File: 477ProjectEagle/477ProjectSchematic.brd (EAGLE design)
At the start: 101.6 x 76.2 mm, 67 parts, among them J1 POWER_JACK_BAT, J2 POWER_JACK_12VOUT, Q1 AO4419, X1 22-23-2051, X10 22-23-2041, X2 XRJK-S-01-6-6-0-2G2-NO

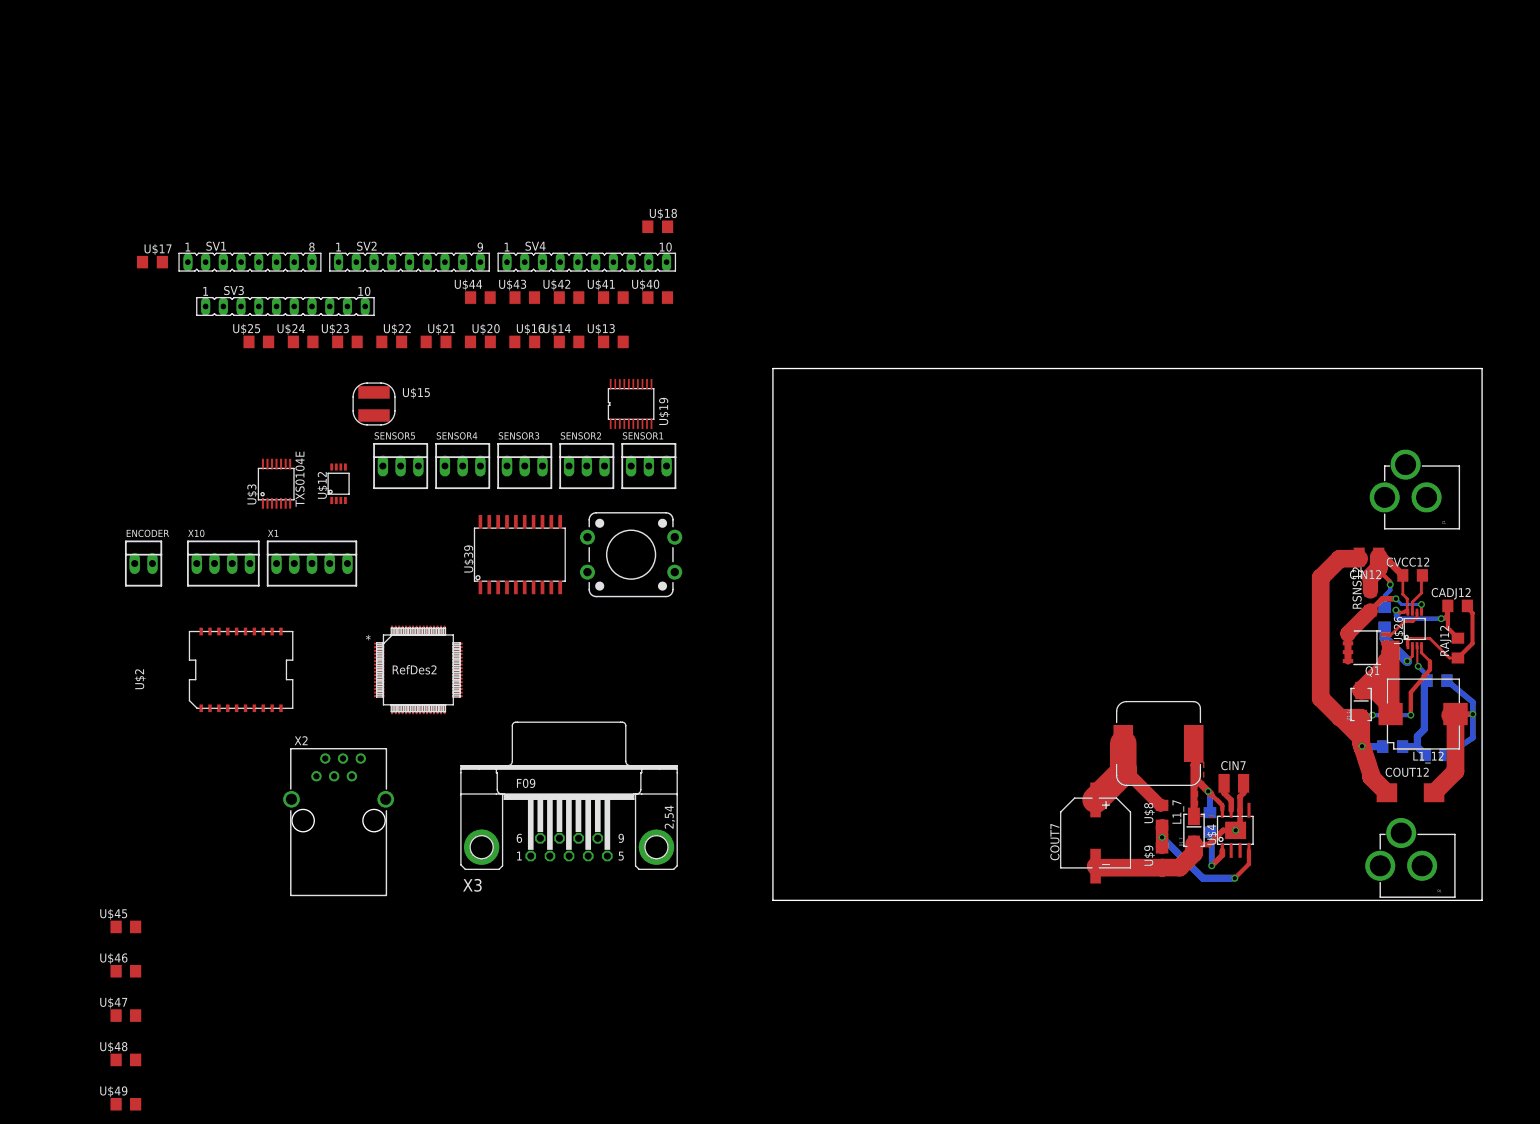
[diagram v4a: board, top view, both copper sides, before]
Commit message: Scott from lab -- worked on main PCB
Got all of the power supply circuits hooked up. Need to review them a
little bit more to make sure all traces are large enough etc...The board
is now 4 inches by 5 inches. That seems to be big enough
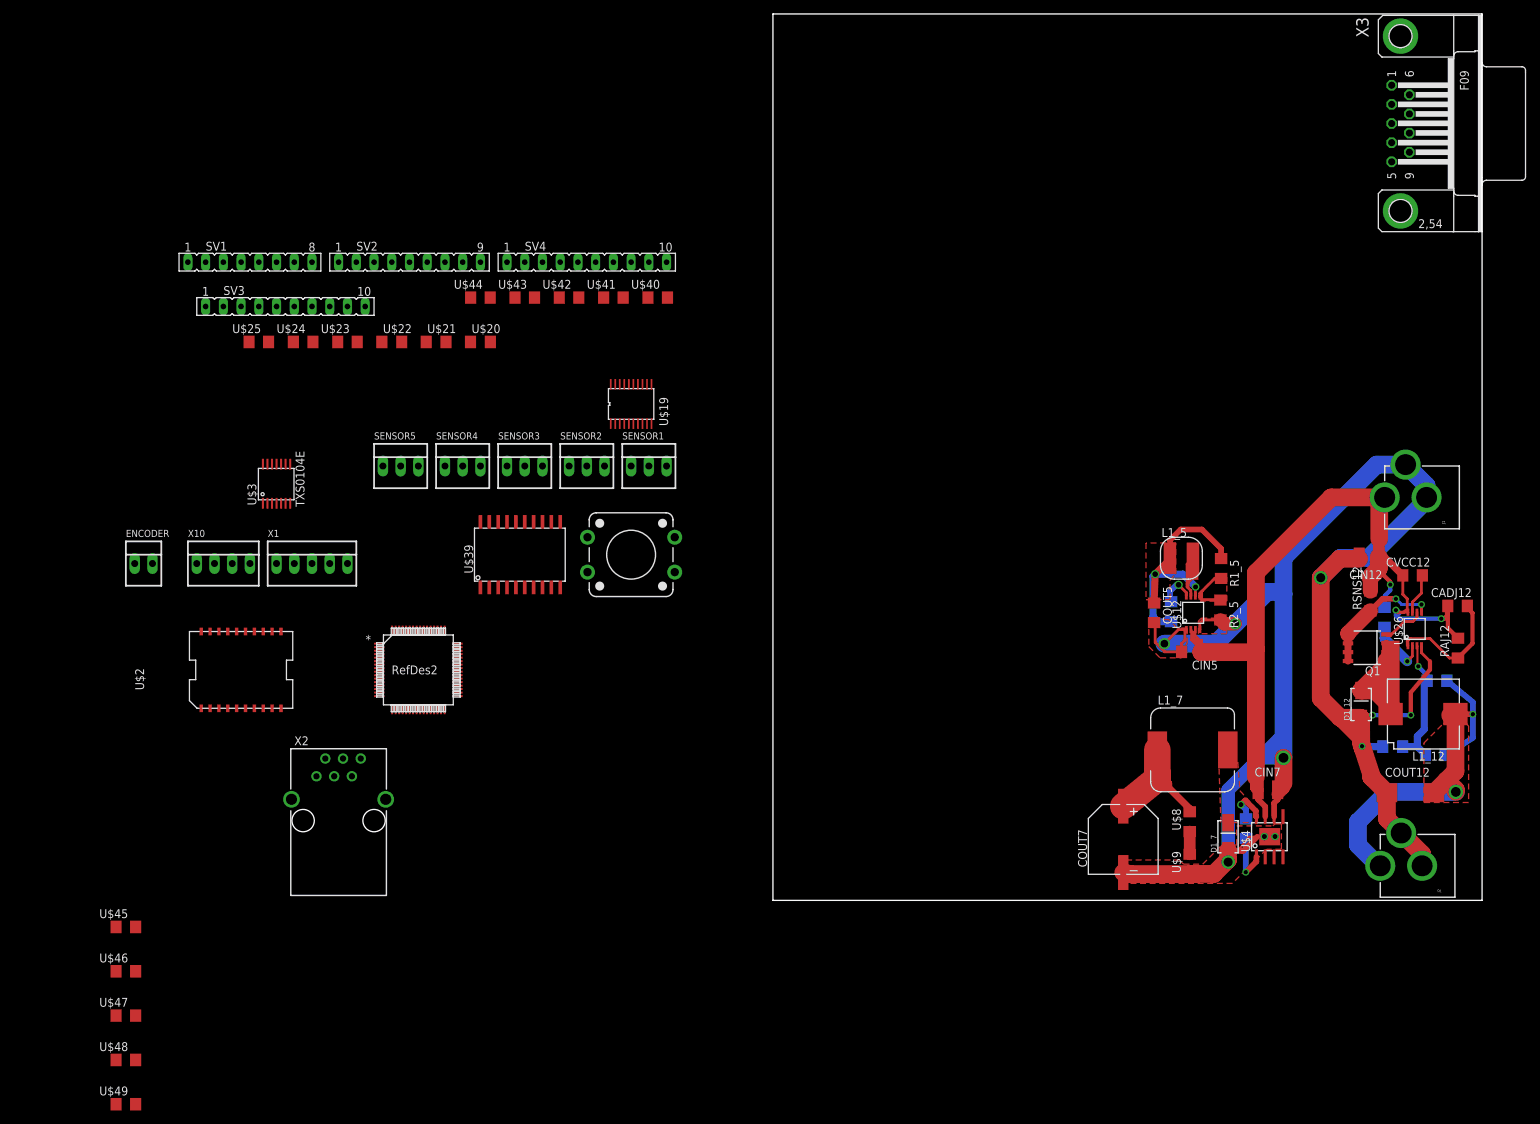
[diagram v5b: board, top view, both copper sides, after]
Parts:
- removed U$13: 10uF, MinotaurParts:C1206
- removed U$14: 22uF, MinotaurParts:C1206
- removed U$15: 2.2uH, MinotaurParts:SDR0403
- removed U$17, U$18: (no value), MinotaurParts:R1206
- added CIN5: 10uF, MinotaurParts:C1206
- added COUT5: 22uF, MinotaurParts:C1206
- added L1_5: 2.2uH, MinotaurParts:SDR0403
- added R1_5, R2_5: (no value), MinotaurParts:R1206
- moved X3 157.9 mm to (89.9, 111.3), turned to 270 degrees
- moved U$12 123.8 mm to (60.2, 41.2)
- moved U$16 100.4 mm to (57.0, 41.4), flipped to the bottom, turned to 90 degrees
- moved CBOOT7 5.26 mm to (67.8, 10.3)
- moved D1_7 4.96 mm to (65.2, 9.12)
- moved L1_7 4.96 mm to (60.1, 21.6)
- moved U$4 4.96 mm to (71.2, 9.12)
- moved CIN7 4.96 mm to (70.9, 15.8)
- moved U$8 4.07 mm to (59.7, 11.3)
- moved U$9 4.07 mm to (59.7, 5.18)
- moved COUT7 4.07 mm to (50.2, 8.74)
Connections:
- net +5V: now also COUT5.1, L1_5.B, R1_5.1; no longer U$14.1, U$15.B, U$17.1
- net GND: now also CIN5.2, COUT5.2, R2_5.2; no longer U$13.2, U$14.2, U$18.2
- net N$36: now also L1_5.A; no longer U$15.A
- net N$40: now also R1_5.2, R2_5.1; no longer U$17.2, U$18.1
- net V+: now also CIN5.1; no longer U$13.1
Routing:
- net GND: track 100.2 -> 267.6 mm, vias 4 -> 8
- net V+: track 44.0 -> 123.2 mm
- net +5V: track 0.00 -> 37.4 mm, vias 0 -> 2
- net +12V: track 31.4 -> 57.1 mm, vias 1 -> 2
- net N$28: track 20.9 -> 3.25 mm, vias 2 -> 0
- net N$16: track 22.4 -> 6.22 mm
- net N$40: track 0.00 -> 8.54 mm
- net N$36: track 0.00 -> 8.53 mm
- net N$37: track 0.00 -> 5.26 mm, vias 0 -> 1
- net +7V: track 17.5 -> 21.2 mm
- added copper zone on layer 1, net +12V
- added copper zone on layer 1, net +5V
- added copper zone on layer 1, net GND
- added copper zone on layer 1, net N$40
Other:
- board size 101.6 x 76.2 mm -> 101.6 x 127 mm

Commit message: Continued work on main PCB
All components are in a rough position on the board. Everything just
needs to be connected now...
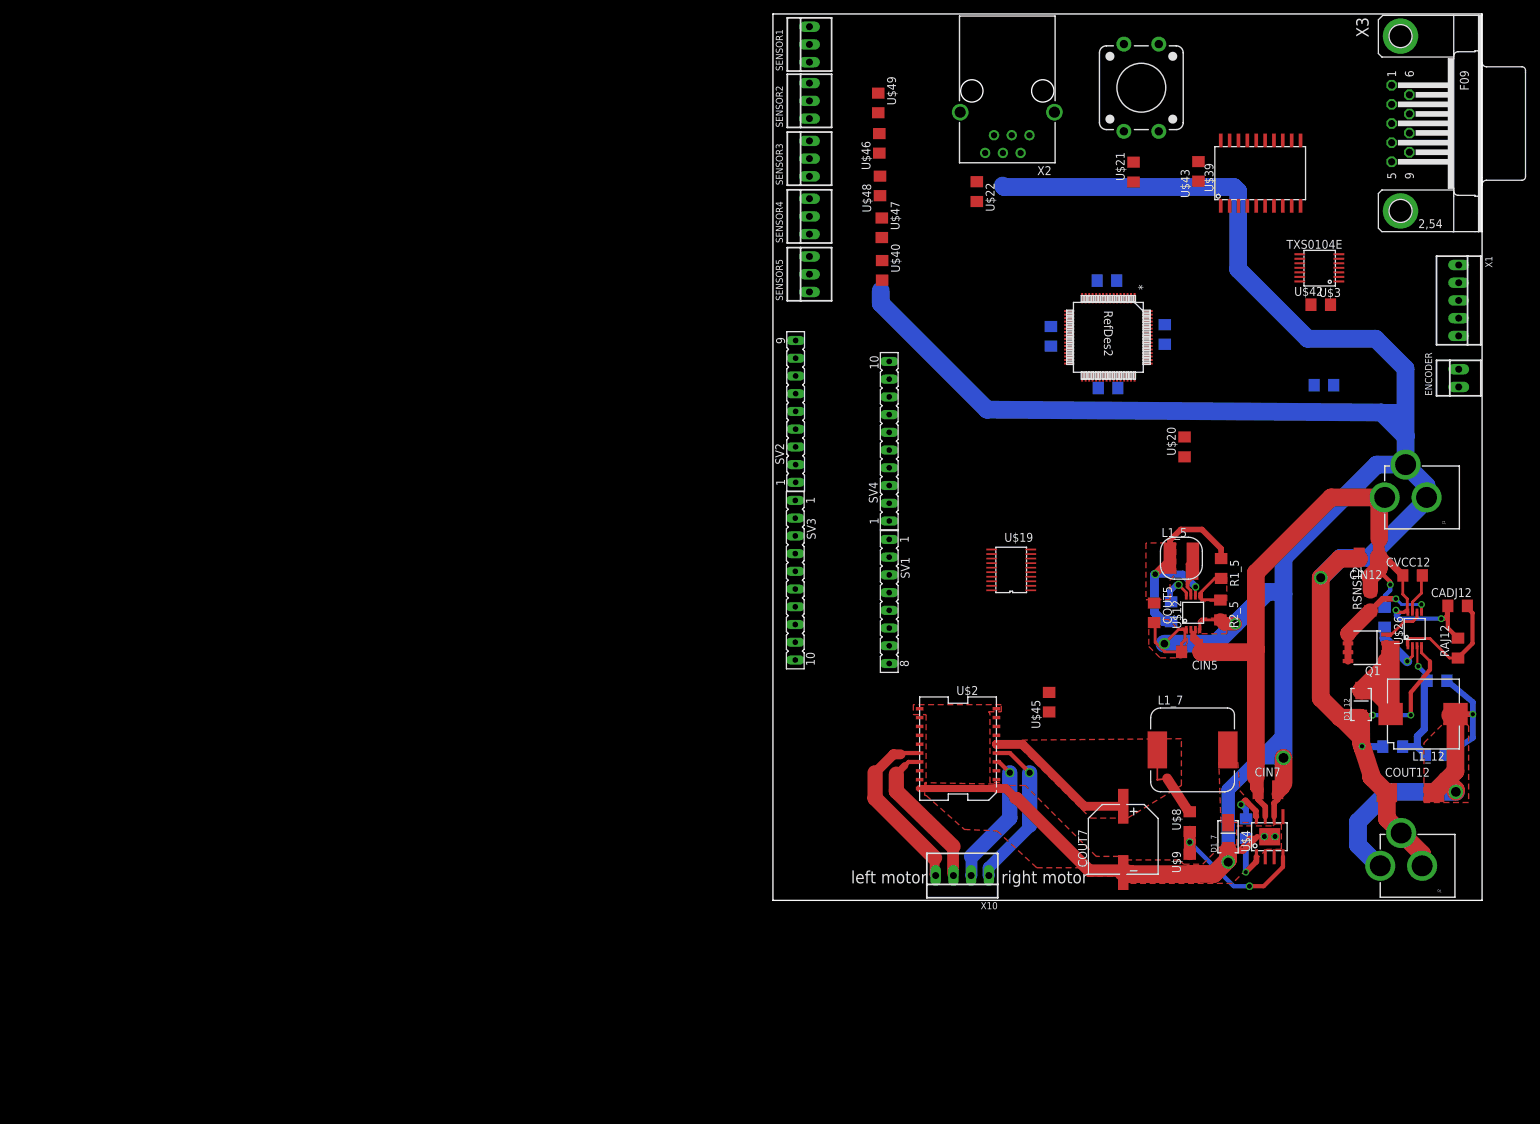
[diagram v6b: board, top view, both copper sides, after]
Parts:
- X10: value 22-23-2041 -> MOTORS
- moved ENCODER 190.3 mm to (98.2, 74.8), turned to 90 degrees
- moved U$49 179.4 mm to (15.1, 114.2), turned to 270 degrees
- moved X1 168.6 mm to (98.2, 86.0), turned to 270 degrees
- moved U$48 165.4 mm to (15.3, 102.4), turned to 90 degrees
- moved U$46 160.4 mm to (15.2, 108.5), turned to 90 degrees
- moved U$47 156.4 mm to (15.6, 96.4), turned to 270 degrees
- moved U$25 152.7 mm to (78.9, 73.8), flipped to the bottom, turned to 180 degrees
- moved U$3 152.6 mm to (78.3, 90.6), turned to 90 degrees
- moved X2 141.8 mm to (33.6, 116.0), turned to 180 degrees
- moved U$45 136.1 mm to (39.6, 28.4), turned to 90 degrees
- moved U$39 119.3 mm to (70.5, 104.2)
- moved U$23 117.1 mm to (56.1, 81.1), flipped to the bottom, turned to 90 degrees
- moved U$24 115.5 mm to (48.0, 73.4), flipped to the bottom, turned to 180 degrees
- moved X10 114.9 mm to (27.1, 3.56), turned to 180 degrees
- moved U$1 109.7 mm to (48.1, 80.7), turned to 270 degrees
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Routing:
- net GND: track 267.6 -> 476.8 mm
- net N$21: track 0.00 -> 25.9 mm
- net N$19: track 0.00 -> 23.1 mm, vias 0 -> 1
- net N$20: track 0.00 -> 22.0 mm
- net N$18: track 0.00 -> 19.6 mm, vias 0 -> 1
- net N$28: track 3.25 -> 21.8 mm, vias 0 -> 2
- net +7V: track 21.2 -> 33.4 mm
- net +5V: track 37.4 -> 32.6 mm
- added copper zone on layer 1, net +7V
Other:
- board text added: "left motor"
- board text added: "right motor"

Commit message: Scott lab -- Work on main PCB
Started connecting everything together. Made a bunch of progress.
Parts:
- moved U$45 67.6 mm to (14.6, 91.2)
- moved U$40 58.6 mm to (73.7, 98.0), flipped to the bottom, turned to 180 degrees
- moved U$25 45.0 mm to (34.7, 82.0), turned to 90 degrees
- moved U$19 41.4 mm to (57.9, 81.3), turned to 270 degrees
- moved U$41 37.2 mm to (85.0, 87.6), flipped to the top
- moved U$23 17.2 mm to (39.3, 84.7), turned to 180 degrees
- moved U$43 16.5 mm to (60.7, 88.0)
- moved U$44 15.9 mm to (54.2, 87.8), flipped to the top
- moved U$20 12.5 mm to (50.2, 73.9), turned to 180 degrees
- moved U$46 11.3 mm to (14.6, 97.2)
- moved U$48 10.7 mm to (14.4, 113.0)
- moved U$1 10.7 mm to (37.4, 81.6)
- moved U$24 10.4 mm to (39.2, 78.9)
- moved U$42 10.0 mm to (86.6, 79.4), turned to 90 degrees
- moved U$3 9.87 mm to (81.6, 81.3), turned to 180 degrees
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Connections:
- net +3V3: now also X1.1; no longer X1.2
- net GND: now also X1.2; no longer X1.1
- net N$12: now also U$3.2
- net N$13: now also U$3.3
- net N$8: now also U$19.A8; no longer U$19.A7
- net N$9: now also U$19.A7; no longer U$19.A8
- net SCL: now also U$3.13
- net SDA: now also U$3.12
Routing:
- net +5V: track 32.6 -> 271.1 mm, vias 2 -> 8
- net GND: track 476.8 -> 674.4 mm, vias 8 -> 13
- net N$42: track 0.00 -> 72.4 mm
- net N$43: track 0.00 -> 69.9 mm
- net +3V3: track 0.00 -> 69.9 mm, vias 0 -> 1
- net N$41: track 0.00 -> 69.0 mm
- net N$44: track 0.00 -> 68.2 mm
- net N$45: track 0.00 -> 67.3 mm
- net N$39: track 0.00 -> 65.5 mm, vias 0 -> 2
- net N$12: track 0.00 -> 60.0 mm, vias 0 -> 2
- net N$13: track 0.00 -> 59.2 mm, vias 0 -> 2
- net N$1: track 0.00 -> 52.7 mm
- net N$2: track 0.00 -> 43.7 mm
- net SCL: track 0.00 -> 40.4 mm, vias 0 -> 1
- net N$3: track 0.00 -> 39.3 mm
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
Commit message: minor changes to main PCB
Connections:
- net N$85: now also U$1.51
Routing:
- net V+: track 123.2 -> 46.3 mm
- net N$5: track 27.0 -> 30.6 mm
- added copper zone on layer 1, net V+
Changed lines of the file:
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@@
 <wire x1="31.7754" y1="82.8294" x2="24.765" y2="82.8294" width="0.3048" layer="1"/>
 <wire x1="24.765" y1="82.8294" x2="17.9832" y2="89.6112" width="0.3048" layer="1"/>
-<wire x1="14.5796" y1="89.786" x2="17.9832" y2="89.6112" width="0" layer="19" extent="1-1"/>
+<wire x1="17.9832" y1="89.6112" x2="14.5796" y2="89.6112" width="0.3048" layer="1"/>
+<wire x1="14.5796" y1="89.6112" x2="14.5796" y2="89.786" width="0.3048" layer="1"/>
 </signal>
 <signal name="N$8">
@@
 <wire x1="83.9948" y1="49.1998" x2="83.9948" y2="48.9428" width="1.778" layer="1"/>
 <wire x1="84.0552" y1="26.289" x2="84.2772" y2="26.067" width="1.778" layer="1"/>
-<wire x1="83.9948" y1="48.9428" x2="81.2008" y2="48.9428" width="2.54" layer="1"/>
 <wire x1="81.2008" y1="48.9428" x2="78.486" y2="46.228" width="2.54" layer="1"/>
 <wire x1="78.486" y1="46.228" x2="78.486" y2="28.956" width="2.54" layer="1"/>
@@
 <wire x1="79.248" y1="82.9056" x2="75.2856" y2="82.9056" width="0.4064" layer="1"/>
 <wire x1="75.2856" y1="82.9056" x2="74.9808" y2="83.2104" width="0.4064" layer="1"/>
+<wire x1="83.9948" y1="48.9428" x2="81.2008" y2="48.9428" width="2.54" layer="1"/>
 <wire x1="54.1528" y1="89.2332" x2="50.2812" y2="110.1836" width="0" layer="19" extent="1-1"/>
 <wire x1="60.6552" y1="89.3856" x2="54.1528" y2="89.2332" width="0" layer="19" extent="1-1"/>
@@
 <wire x1="86.8172" y1="47.2694" x2="86.8172" y2="46.863" width="0.6096" layer="1"/>
 <wire x1="89.548" y1="41.2874" x2="90.973" y2="41.2874" width="0.4064" layer="1"/>
-<wire x1="86.7948" y1="49.1998" x2="86.7948" y2="48.4632" width="2.54" layer="1"/>
-<wire x1="86.7948" y1="48.4632" x2="86.7948" y2="47.5518" width="2.54" layer="1"/>
-<wire x1="86.7948" y1="47.5518" x2="85.598" y2="46.355" width="2.54" layer="1"/>
-<wire x1="85.598" y1="46.355" x2="85.598" y2="44.3226" width="2.1844" layer="1"/>
 <wire x1="70.5358" y1="11.9936" x2="70.5358" y2="13.4366" width="0.8128" layer="1"/>
 <wire x1="70.5358" y1="13.4366" x2="69.5198" y2="14.4526" width="0.8128" layer="1"/>
 <wire x1="69.5198" y1="14.4526" x2="69.5198" y2="15.8466" width="0.8128" layer="1"/>
 <wire x1="69.5198" y1="15.8466" x2="69.5168" y2="15.8496" width="0.8128" layer="1"/>
-<wire x1="87.646" y1="57.7342" x2="86.868" y2="57.7342" width="2.54" layer="1"/>
-<wire x1="86.868" y1="57.7342" x2="86.868" y2="51.816" width="2.54" layer="1"/>
-<wire x1="86.868" y1="51.816" x2="86.7948" y2="51.816" width="1.6764" layer="1"/>
-<wire x1="86.7948" y1="51.816" x2="86.7948" y2="48.4632" width="1.6764" layer="1"/>
-<wire x1="86.868" y1="57.7342" x2="79.9846" y2="57.7342" width="2.54" layer="1"/>
-<wire x1="79.9846" y1="57.7342" x2="69.1896" y2="46.9392" width="2.54" layer="1"/>
-<wire x1="69.1896" y1="46.9392" x2="69.1896" y2="35.9664" width="2.54" layer="1"/>
-<wire x1="69.1896" y1="35.9664" x2="69.1896" y2="17.6784" width="2.54" layer="1"/>
-<wire x1="69.1896" y1="17.6784" x2="69.1896" y2="16.1768" width="1.6764" layer="1"/>
-<wire x1="69.1896" y1="16.1768" x2="69.5168" y2="15.8496" width="1.6764" layer="1"/>
 <wire x1="61.344" y1="35.6108" x2="61.344" y2="35.8872" width="0.3048" layer="1"/>
 <wire x1="61.344" y1="35.8872" x2="59.944" y2="37.2872" width="0.3048" layer="1"/>
@@
 <wire x1="61.468" y1="37.2872" x2="61.468" y2="35.7348" width="0.3048" layer="1"/>
 <wire x1="61.468" y1="35.7348" x2="61.344" y2="35.6108" width="0.3048" layer="1"/>
-<wire x1="68.7832" y1="35.56" x2="61.3948" y2="35.56" width="2.54" layer="1"/>
-<wire x1="61.3948" y1="35.56" x2="61.344" y2="35.6108" width="2.54" layer="1"/>
-<wire x1="68.7832" y1="35.56" x2="69.1896" y2="35.9664" width="2.54" layer="1"/>
-<wire x1="86.7948" y1="47.5518" x2="86.8172" y2="47.2694" width="0" layer="19" extent="1-1"/>
+<polygon width="0.3048" layer="1" thermals="no">
+<vertex x="86.1568" y="50.3936"/>
+<vertex x="86.1568" y="47.8028"/>
+<vertex x="84.0232" y="46.0248"/>
+<vertex x="84.0232" y="43.5864"/>
+<vertex x="86.4616" y="43.5864"/>
+<vertex x="86.5124" y="45.0088"/>
+<vertex x="90.7796" y="45.0088"/>
+<vertex x="90.7796" y="47.4472"/>
+<vertex x="90.678" y="47.5488"/>
+<vertex x="90.5256" y="47.5488"/>
+<vertex x="87.63" y="50.4444"/>
+<vertex x="86.2076" y="50.4444"/>
+</polygon>
+<wire x1="87.6016" y1="49.1998" x2="87.646" y2="57.7342" width="0" layer="19" extent="1-1"/>
+<wire x1="61.468" y1="37.2872" x2="85.598" y2="44.3226" width="0" layer="19" extent="1-1"/>
+<wire x1="69.5168" y1="15.8496" x2="61.344" y2="35.6108" width="0" layer="19" extent="1-1"/>
 </signal>
 <signal name="N$6">
@@
 <signal name="N$85">
 <contactref element="SV3" pad="10"/>
+<contactref element="U$1" pad="51"/>
+<wire x1="3.2004" y1="34.4424" x2="43.0022" y2="78.8416" width="0" layer="19" extent="1-1"/>
 </signal>
 <signal name="N$86">
